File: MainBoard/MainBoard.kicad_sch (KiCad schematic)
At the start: 45 parts, among them U1 TL074CN

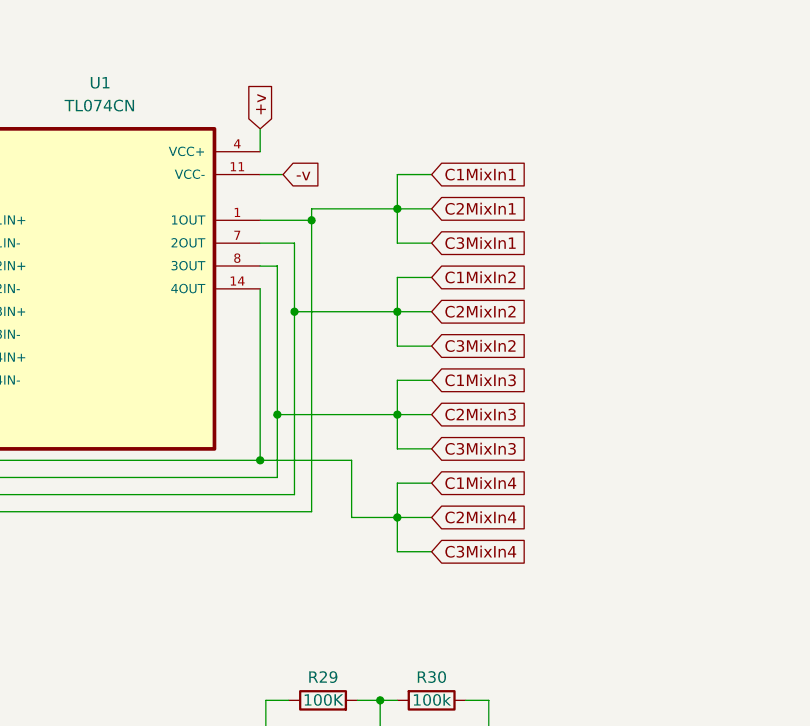
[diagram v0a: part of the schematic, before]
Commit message: corrected duplicate annotations, simplified signal path, passes all DRC checks
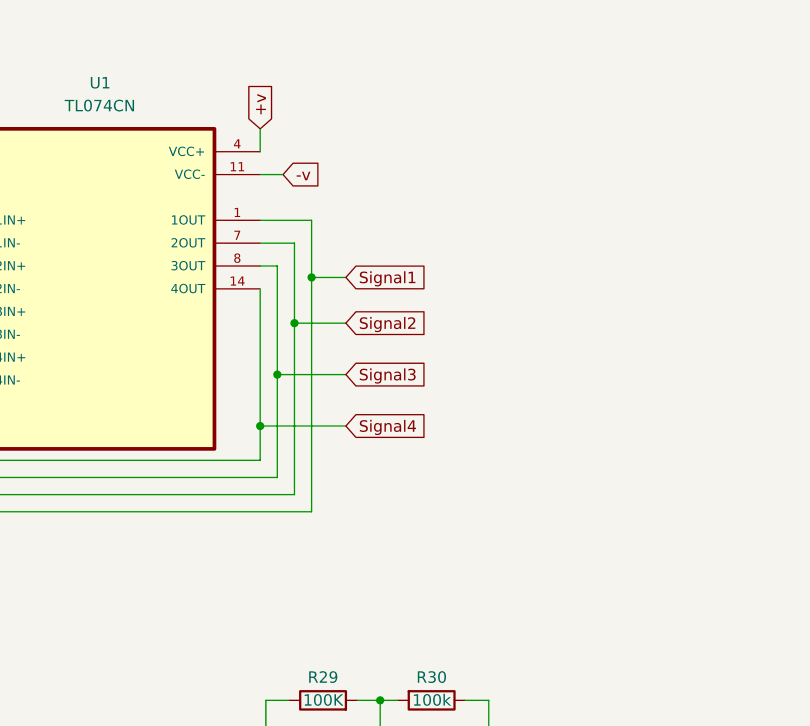
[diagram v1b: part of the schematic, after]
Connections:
- net C1MixIn1 renamed Signal1
- net C1MixIn2 renamed Signal2
- net C1MixIn3 renamed Signal3
- net C1MixIn4 renamed Signal4
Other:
- company: (none) -> R-mods
- title: (none) -> Matrix Mixer

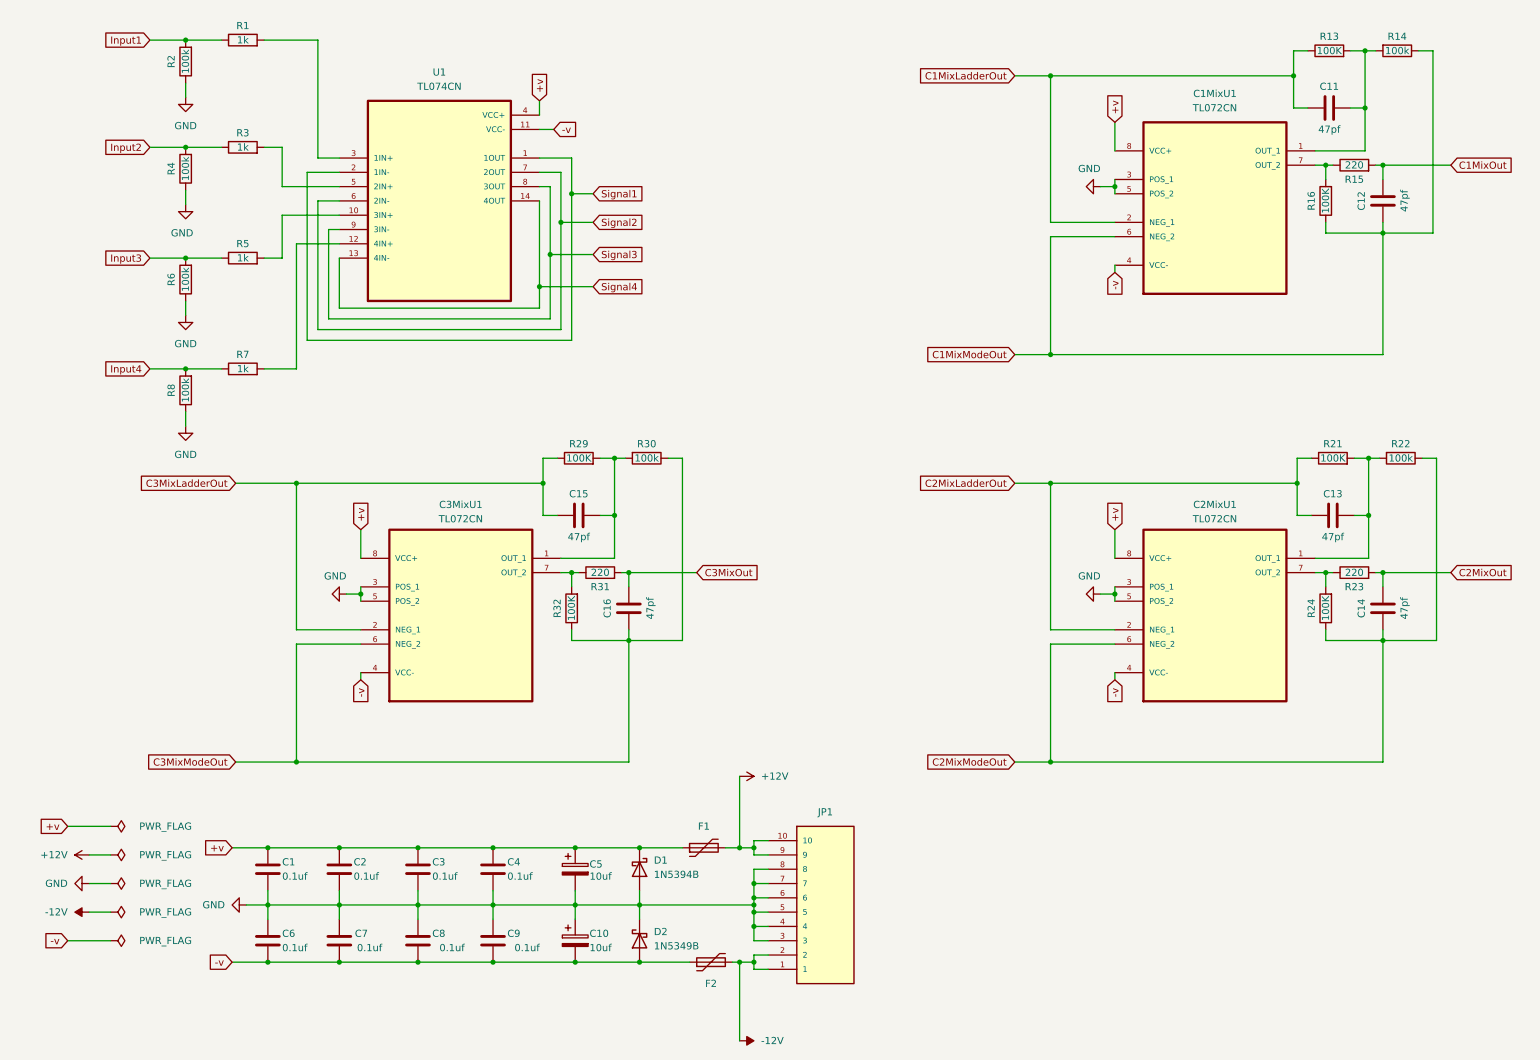
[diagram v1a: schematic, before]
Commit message: laid out MainBoard, added 3d models
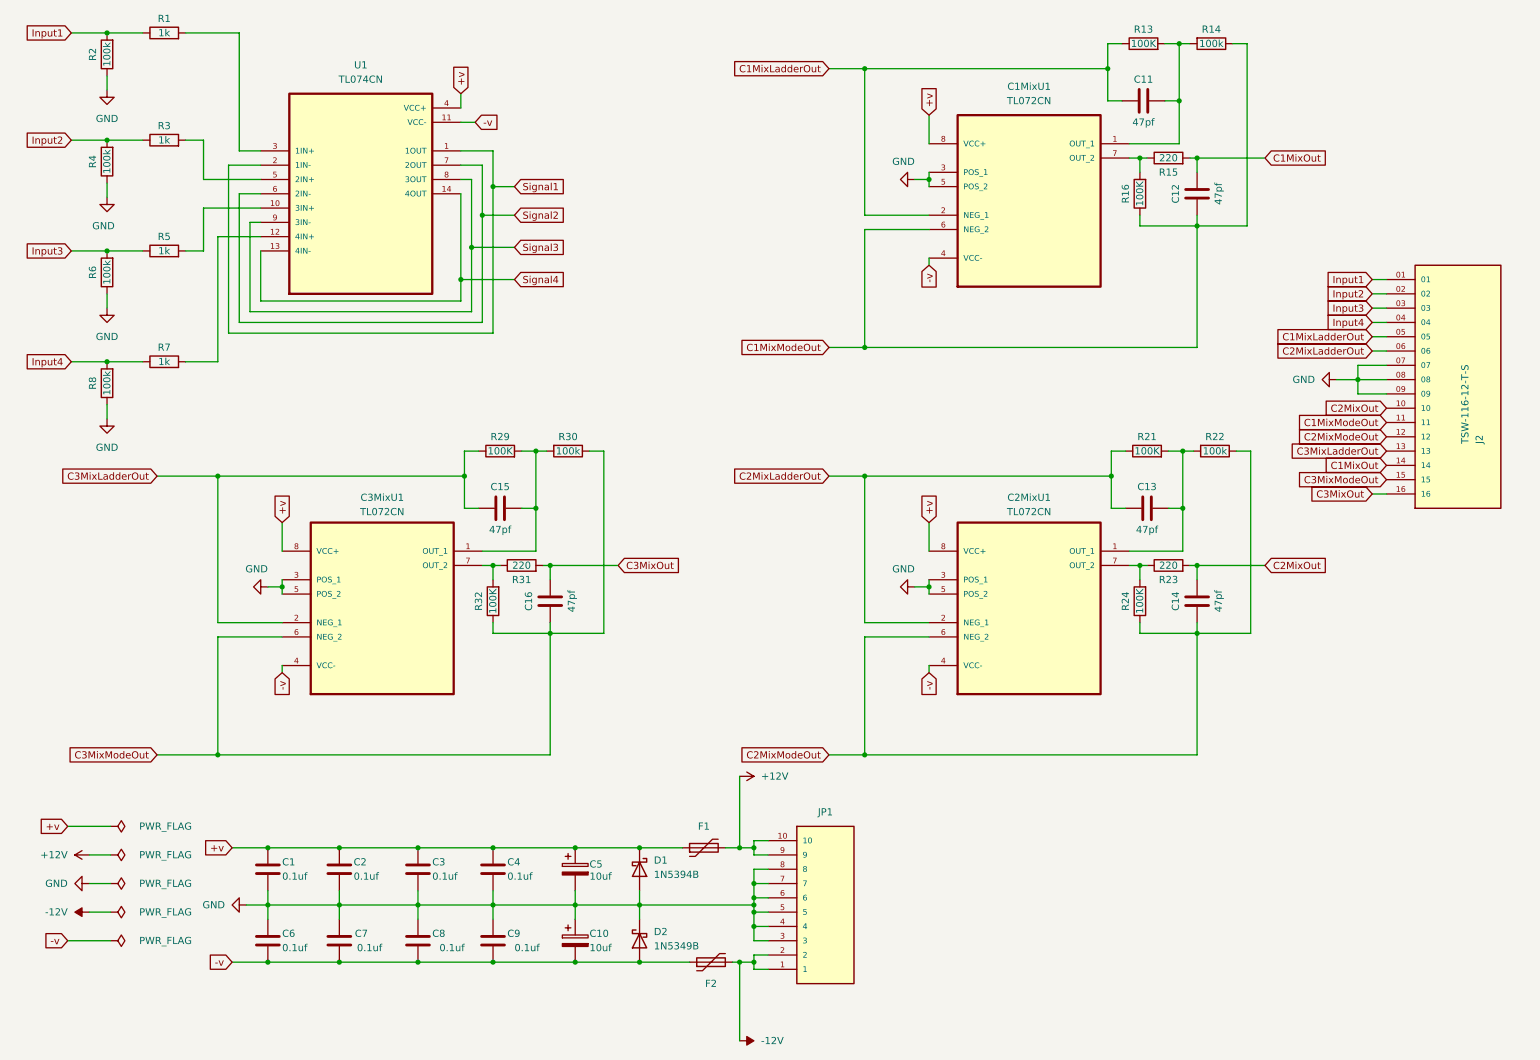
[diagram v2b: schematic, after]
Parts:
- added J2: TSW-116-12-T-S, TSW-116-12-T-S:SAMTEC_TSW-116-12-T-S, symbol TSW-116-12-T-S:TSW-116-12-T-S
- C11, C12, C13, C14, C15, C16: footprint (none) -> Capacitor_THT:C_Disc_D7.5mm_W4.4mm_P5.00mm
- R1, R13, R14, R15, R16, R2, R21, R22, R23, R24, R29, R3, R30, R31, R32, R4, R5, R6, R7, R8: footprint (none) -> Resistor_THT:R_Axial_DIN0207_L6.3mm_D2.5mm_P10.16mm_Horizontal
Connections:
- net C1MixLadderOut: now also J2.05
- net C1MixModeOut: now also J2.11
- net C1MixOut: now also J2.14
- net C2MixLadderOut: now also J2.06
- net C2MixModeOut: now also J2.12
- net C2MixOut: now also J2.10
- net C3MixLadderOut: now also J2.13
- net C3MixModeOut: now also J2.15
- net C3MixOut: now also J2.16
- net GND: now also J2.07, J2.08, J2.09
- net Input1: now also J2.01
- net Input2: now also J2.02
- net Input3: now also J2.03
- net Input4: now also J2.04
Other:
- moved on the sheet: C11, C12, C13, C14, C15, C16, C1MixU1, C2MixU1, C3MixU1, R1, R13, R14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

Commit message: added footprints and 3dmodels
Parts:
- removed C1, C6: 0.1uf, Capacitor_THT:C_Disc_D7.5mm_W4.4mm_P5.00mm, symbol Device:C
- removed R1, R3, R5, R7: 1k, Resistor_THT:R_Axial_DIN0207_L6.3mm_D2.5mm_P10.16mm_Horizontal, symbol Device:R
- removed R2, R4, R6, R8: 100k, Resistor_THT:R_Axial_DIN0207_L6.3mm_D2.5mm_P10.16mm_Horizontal, symbol Device:R
- removed U1: TL074CN, TL074CN:DIP794W45P254L1969H508Q14, symbol TL074CN:TL074CN
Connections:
- net Input1 is gone; now on net C1MixLadderOut: J2.01
- net Input2 is gone; now on net C1MixModeOut: J2.02
- net Input3 is gone; now on net C1MixOut: J2.03
- net Input4 is gone; now on net C2MixLadderOut: J2.04
- net +v: now also J2.12
- net -v: now also J2.11
- net C1MixLadderOut: no longer J2.05
- net C1MixModeOut: no longer J2.11
- net C1MixOut: no longer J2.14
- net C2MixLadderOut: no longer J2.06
- net C2MixModeOut: now also J2.05; no longer J2.12
- net C2MixOut: now also J2.13; no longer J2.10
- net C3MixLadderOut: now also J2.14; no longer J2.13
- net GND: now also J2.06, J2.10
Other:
- moved on the sheet: C11, C12, C13, C14, C1MixU1, C2MixU1, J2, R13, R14, R15, R16, R21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

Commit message: updated 200 ohm resister on output to 1k for more reverse protection
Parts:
- R15, R23, R31: value 220 -> 1k
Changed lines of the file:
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@@
 			)
 		)
-		(property "Value" "220"
+		(property "Value" "1k"
 			(at 102.87 111.125 90)
 			(effects
@@
 			)
 		)
-		(property "Value" "220"
+		(property "Value" "1k"
 			(at 98.425 41.275 90)
 			(effects
@@
 			)
 		)
-		(property "Value" "220"
+		(property "Value" "1k"
 			(at 235.585 41.275 90)
 			(effects
